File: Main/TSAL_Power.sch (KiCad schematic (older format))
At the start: 124 parts, among them Q10 NPN, Q11 MJD122, Q12 PNP, Q6 BSC0904NSI, Q7 BSC0902NSI, Q8 BSC0902NSI, Q9 MJD122, U10 TLV431, U11 TLV431, U4 TPS562200, U5 TPS63020, U6 MAX40200AUK, U7 INA180A3, U8 TLV9104, U9 LM25117

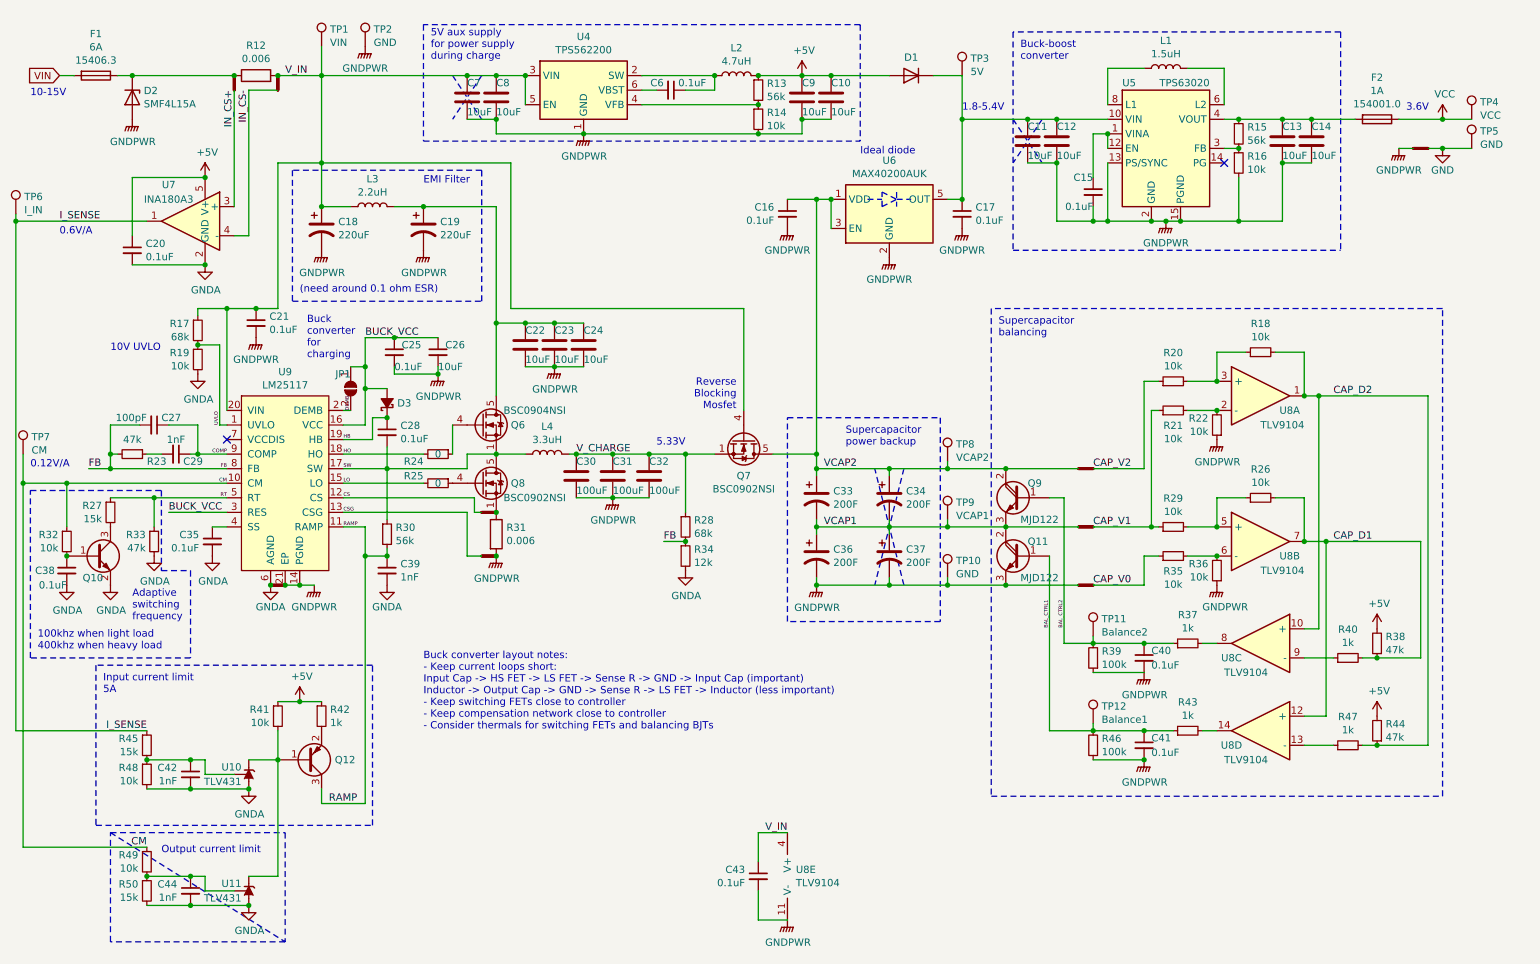
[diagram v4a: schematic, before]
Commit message: Main: optimized layout
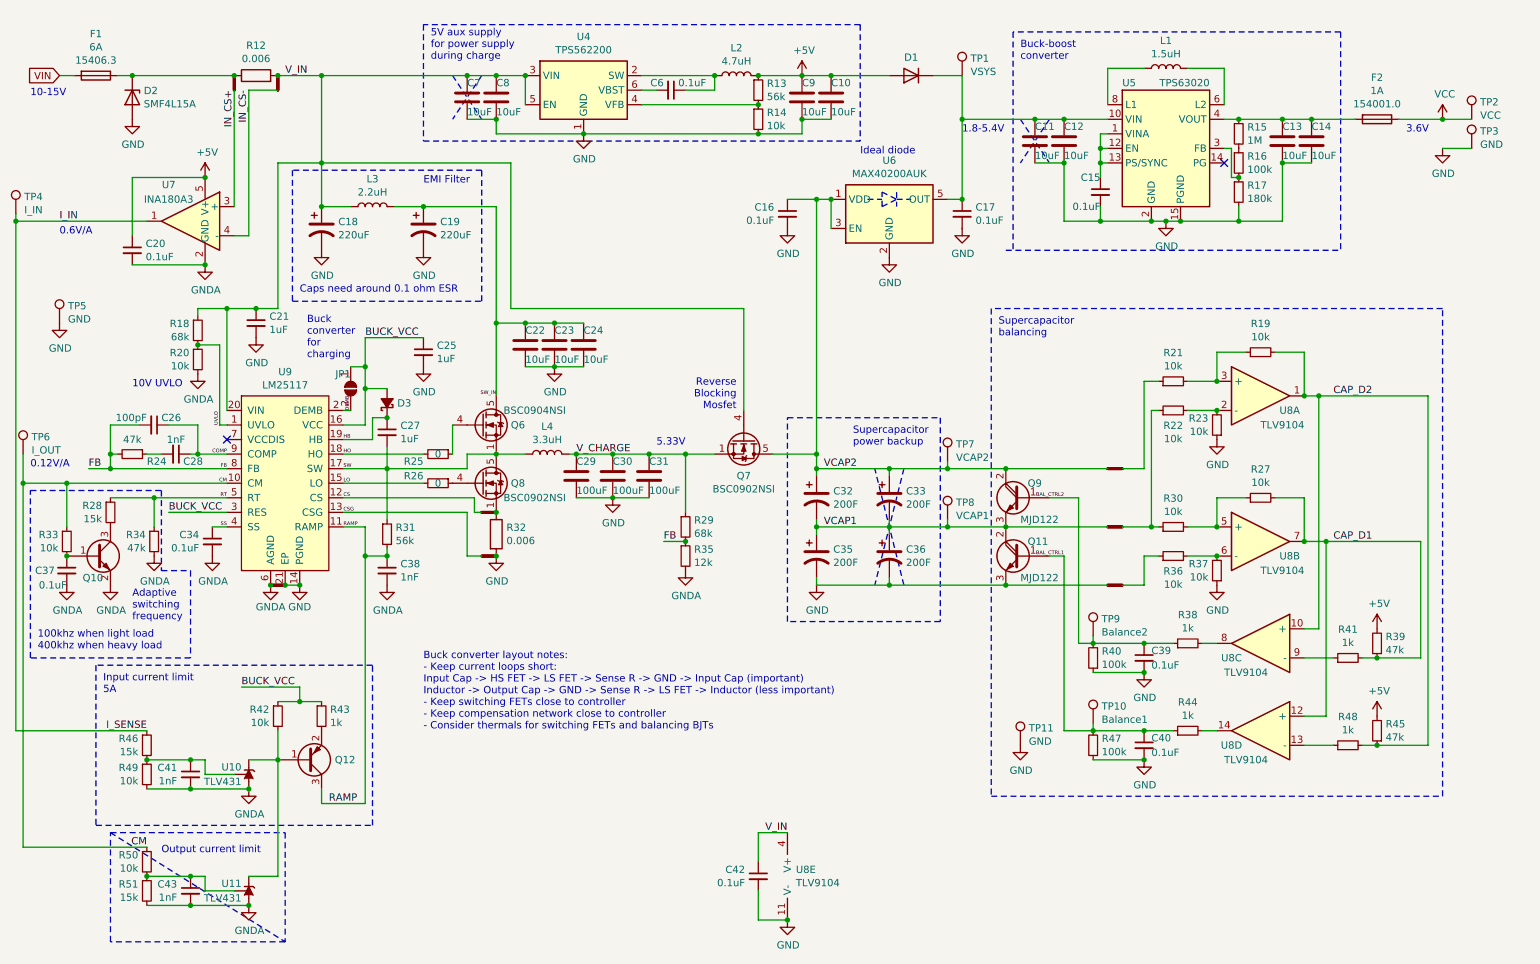
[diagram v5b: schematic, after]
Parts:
- removed C25, C28: 0.1uF, Capacitor_SMD:C_0402_1005Metric, symbol Device:C_Small
- removed TP1, TP10, TP2, TP9: ~, TestPoint:TestPoint_Loop_D2.50mm_Drill1.0mm, symbol Connector:TestPoint
- removed ZZ4, ZZ6, ZZ9: ~, project:Trace_0.2mmx0.6mm, symbol project:Wire
- added C27: 1uF, Capacitor_SMD:C_0402_1005Metric, symbol Device:C_Small
- added R16: 100k, Resistor_SMD:R_0805_2012Metric, symbol Device:R_Small
- added TP11, TP5, TP7: ~, TestPoint:TestPoint_Loop_D2.50mm_Drill1.0mm, symbol Connector:TestPoint
- added ZZ5, ZZ8: ~, project:Trace_0.2mmx0.6mm, symbol project:Wire
- C21: value 0.1uF -> 1uF; Comment (none) -> 25V
- C25: renamed from C26; value 10uF -> 1uF; footprint Capacitor_SMD:C_0805_2012Metric -> Capacitor_SMD:C_0402_1005Metric; Comment (none) -> 25V
- R13, R14: footprint Resistor_SMD:R_0805_2012Metric -> Resistor_SMD:R_0402_1005Metric
- R15: value 56k -> 1M
- R17: renamed from R16; value 10k -> 180k
- R20: renamed from R19; footprint Resistor_SMD:R_0805_2012Metric -> Resistor_SMD:R_0402_1005Metric
- R31: renamed from R30; footprint Resistor_SMD:R_0805_2012Metric -> Resistor_SMD:R_0402_1005Metric
- R49: renamed from R48; footprint Resistor_SMD:R_0805_2012Metric -> Resistor_SMD:R_0402_1005Metric
- R50: renamed from R49; footprint Resistor_SMD:R_0805_2012Metric -> Resistor_SMD:R_0402_1005Metric
- TP1: renamed from TP3; Comment 5V -> VSYS
- TP6: renamed from TP7; Comment CM -> I_OUT
- TP8: Comment VCAP2 -> VCAP1
- ZZ3: footprint project:Trace_1mmx2mm -> project:Trace_0.2mmx0.6mm
- ZZ7: renamed from ZZ8; footprint project:Trace_0.4mmx0.8mm -> project:Trace_0.2mmx0.6mm
- renumbered C27 to C26, C29 to C28, C30 to C29, C31 to C30, C32 to C31, C33 to C32, C34 to C33, C35 to C34, C36 to C35, C37 to C36, C38 to C37, C39 to C38, C40 to C39, C41 to C40, C42 to C41, C43 to C42, C44 to C43, R17 to R18, R18 to R19, R20 to R21, R21 to R22, R22 to R23, R23 to R24, R24 to R25, R25 to R26, R26 to R27, R27 to R28, R28 to R29, R29 to R30, R31 to R32, R32 to R33, R33 to R34, R34 to R35, R35 to R36, R36 to R37, R37 to R38, R38 to R39, R39 to R40, R40 to R41, R41 to R42, R42 to R43, R43 to R44, R44 to R45, R45 to R46, R46 to R47, R47 to R48, R50 to R51, TP12 to TP10, TP4 to TP2, TP5 to TP3, TP6 to TP4, TP11 to TP9, ZZ5 to ZZ4, ZZ7 to ZZ6
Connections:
- net +5V: no longer R42.1, R43.1
- net BUCK_VCC: now also R42.1, R43.1
- net GND: now also C10.2, C11.2, C12.2, C13.2, C14.2, C15.2, C16.2, C17.2, C18.2, C19.2, C21.2, C22.2, C23.2, C24.2, C25.2, C29.2, C30.2, C31.2, C35.2, C36.2, C39.2, C40.2, C42.2, C7.2, C8.2, C9.2, D2.2 (A), Q11.3 (E), R14.2, R17.2, R23.1, R32.2, R37.1, R40.1, R47.1, U4.1 (GND), U5.15 (PGND), U5.2 (GND), U6.2 (GND), U8.11 (V-), U9.14 (PGND), U9.21 (EP), ZZ6.2, ZZ7.2, TP11.1, TP5.1, ZZ8.1; no longer ZZ3.2
- net HB: now also C27.1
- net SW: now also C27.2
- net VCAP1: now also TP8.1, ZZ5.1
- net VCAP2: now also ZZ3.1, TP7.1; no longer TP8.1
- net SW_IN: now reaches C19.1, C22.1, C23.1, C24.1, L3.2, Q6.5 (D)
- net SS: now reaches C34.1, U9.4 (SS)
- net at C15.1, U5.1 (VINA), U5.12 (EN): now also U5.13 (PS/SYNC)
- net at R17.1, U5.3 (FB): now also R16.2; no longer R15.2
- net CAP_V0: no longer names the net of R36.1
- net CAP_V0: now also ZZ8.2
- net CAP_V1: no longer names the net of R22.1, R30.1
- net CAP_V1: now also ZZ5.2
- net CAP_V2: no longer names the net of R21.1
- net CAP_V2: now also ZZ3.2
- removed net GNDPWR: C10.2, C11.2, C12.2, C13.2, C14.2, C15.2, C16.2, C17.2, C18.2, C19.2, C21.2, C22.2, C23.2, C24.2, C25.2, C29.2, C30.2, C31.2, C35.2, C36.2, C39.2, C40.2, C42.2, C7.2, C8.2, C9.2, D2.2 (A), Q11.3 (E), R14.2, R17.2, R23.1, R32.2, R37.1, R40.1, R47.1, U4.1 (GND), U5.13 (PS/SYNC), U5.15 (PGND), U5.2 (GND), U6.2 (GND), U8.11 (V-), U9.14 (PGND), U9.21 (EP), ZZ3.1, ZZ6.2, ZZ7.2
- net I_SENSE renamed I_IN
- new net: R15.2, R16.1
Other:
- note added: "Caps need around 0.1 ohm ESR"
- note removed: "(need around 0.1 ohm ESR)"
- moved on the sheet: C11, C12, C15, C25, R17

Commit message: Main: fix rescue symbols
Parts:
- C18, C19, C32, C33, C35, C36: symbol TSAL-rescue:C_Polarized_US-Device -> Device:C_Polarized
- D3: symbol TSAL-rescue:D_Schottky_Small_Filled-Device -> Device:D_Schottky_Small_Filled
- U8: symbol TSAL-rescue:Opamp_Quad-Device -> Device:Opamp_Quad
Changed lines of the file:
@@
 $EndComp
 $Comp
-L TSAL-rescue:Opamp_Quad-Device U8
+L Device:Opamp_Quad U8
 U 3 1 616C69E2
 P 9250 5400
+AR Path="/616C69E2" Ref="U8"  Part="3"
+AR Path="/5DE07D62/616C69E2" Ref="U8"  Part="3"
 F 0 "U8" H 9450 5300 50  0000 C CNN
 F 1 "TLV9104" H 9350 5200 50  0000 C CNN
@@
 $EndComp
 $Comp
-L TSAL-rescue:Opamp_Quad-Device U8
+L Device:Opamp_Quad U8
 U 4 1 616C7F69
 P 9250 6000
+AR Path="/616C7F69" Ref="U8"  Part="4"
+AR Path="/5DE07D62/616C7F69" Ref="U8"  Part="4"
 F 0 "U8" H 9450 5900 50  0000 C CNN
 F 1 "TLV9104" H 9350 5800 50  0000 C CNN
@@
 $EndComp
 $Comp
-L TSAL-rescue:Opamp_Quad-Device U8
+L Device:Opamp_Quad U8
 U 2 1 616C4A34
 P 9250 4700
+AR Path="/616C4A34" Ref="U8"  Part="2"
+AR Path="/5DE07D62/616C4A34" Ref="U8"  Part="2"
 F 0 "U8" H 9450 4600 50  0000 C CNN
 F 1 "TLV9104" H 9400 4500 50  0000 C CNN
@@
 $EndComp
 $Comp
-L TSAL-rescue:Opamp_Quad-Device U8
+L Device:Opamp_Quad U8
 U 1 1 615ADA58
 P 9250 3700
+AR Path="/615ADA58" Ref="U8"  Part="1"
+AR Path="/5DE07D62/615ADA58" Ref="U8"  Part="1"
 F 0 "U8" H 9450 3600 50  0000 C CNN
 F 1 "TLV9104" H 9400 3500 50  0000 C CNN
@@
 $EndComp
 $Comp
-L TSAL-rescue:Opamp_Quad-Device U8
+L Device:Opamp_Quad U8
 U 5 1 616A1882
 P 6100 7000
+AR Path="/616A1882" Ref="U8"  Part="5"
+AR Path="/5DE07D62/616A1882" Ref="U8"  Part="5"
 F 0 "U8" H 6058 7046 50  0000 L CNN
 F 1 "TLV9104" H 6058 6955 50  0000 L CNN
@@
 $EndComp
 $Comp
-L TSAL-rescue:D_Schottky_Small_Filled-Device D3
+L Device:D_Schottky_Small_Filled D3
 U 1 1 602CFF2F
 P 3250 3750
+AR Path="/602CFF2F" Ref="D3"  Part="1"
+AR Path="/5DE07D62/602CFF2F" Ref="D3"  Part="1"
 F 0 "D3" V 3250 3680 50  0000 R CNN
 F 1 "~" V 3205 3680 50  0000 R CNN
@@
 $EndComp
 $Comp
-L TSAL-rescue:C_Polarized_US-Device C?
+L Device:C_Polarized C?
 U 1 1 60398AFC
 P 6200 4400
@@
 $EndComp
 $Comp
-L TSAL-rescue:C_Polarized_US-Device C?
+L Device:C_Polarized C?
 U 1 1 60399785
 P 6200 4800
@@
 $EndComp
 $Comp
-L TSAL-rescue:C_Polarized_US-Device C?
+L Device:C_Polarized C?
 U 1 1 6039DE0A
 P 6700 4400
@@
 $EndComp
 $Comp
-L TSAL-rescue:C_Polarized_US-Device C?
+L Device:C_Polarized C?
 U 1 1 6039DE10
 P 6700 4800
@@
 $EndComp
 $Comp
-L TSAL-rescue:C_Polarized_US-Device C?
+L Device:C_Polarized C?
 U 1 1 604522CD
 P 2800 2550
@@
 $EndComp
 $Comp
-L TSAL-rescue:C_Polarized_US-Device C?
+L Device:C_Polarized C?
 U 1 1 6136B917
 P 3500 2550

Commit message: Main: update sot23-5/6 footprints
Bloody kicad libaries
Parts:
- F1, F2: footprint footprints_archive_old_design:Fuseholder_Littelfuse_Nano2_154x -> Fuse:Fuseholder_Littelfuse_Nano2_154x
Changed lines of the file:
@@
 F 0 "F2" V 9763 1800 50  0000 C CNN
 F 1 "1A" V 9854 1800 50  0000 C CNN
-F 2 "footprints_archive_old_design:Fuseholder_Littelfuse_Nano2_154x" V 9980 1800 50  0001 C CNN
+F 2 "Fuse:Fuseholder_Littelfuse_Nano2_154x" V 9980 1800 50  0001 C CNN
 F 3 "~" H 10050 1800 50  0001 C CNN
 F 4 "154001.0" V 9945 1800 50  0000 C CNN "Part"
@@
 F 0 "F1" V 963 1500 50  0000 C CNN
 F 1 "6A" V 1054 1500 50  0000 C CNN
-F 2 "footprints_archive_old_design:Fuseholder_Littelfuse_Nano2_154x" V 1180 1500 50  0001 C CNN
+F 2 "Fuse:Fuseholder_Littelfuse_Nano2_154x" V 1180 1500 50  0001 C CNN
 F 3 "~" H 1250 1500 50  0001 C CNN
 F 4 "15406.3" V 1145 1500 50  0000 C CNN "Part"

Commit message: Main: archive symbols and footprints
Kicad library management is really terrible.
This is pulled together with janky scripts and sed.
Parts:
- C10, C11, C12, C13, C14, C9: footprint Capacitor_SMD:C_0805_2012Metric -> archive:C_0805_2012Metric; symbol Device:C -> archive:Device_C
- C15, C16, C17, C20, C21, C25, C26, C27, C28, C34, C37, C38, C39, C40, C41, C42, C43, C6: footprint Capacitor_SMD:C_0402_1005Metric -> archive:C_0402_1005Metric; symbol Device:C_Small -> archive:Device_C_Small
- C18, C19: footprint Capacitor_SMD:CP_Elec_8x10.5 -> archive:CP_Elec_8x10.5; symbol Device:C_Polarized -> archive:Device_C_Polarized
- C22, C23, C24, C29, C30, C31, C7, C8: footprint Capacitor_SMD:C_1210_3225Metric -> archive:C_1210_3225Metric; symbol Device:C -> archive:Device_C
- C32, C33, C35, C36: footprint Capacitor_THT:CP_Radial_D30.0mm_P10.00mm_SnapIn -> archive:CP_Radial_D30.0mm_P10.00mm_SnapIn; symbol Device:C_Polarized -> archive:Device_C_Polarized
- D1: footprint Diode_SMD:D_SOD-123 -> archive:D_SOD-123; symbol Device:D -> archive:Device_D
- D2: footprint Diode_SMD:D_SOD-123 -> archive:D_SOD-123; symbol Device:D_Zener -> archive:Device_D_Zener
- D3: footprint Diode_SMD:D_SOD-323 -> archive:D_SOD-323; symbol Device:D_Schottky_Small_Filled -> archive:Device_D_Schottky_Small_Filled
- F1, F2: footprint Fuse:Fuseholder_Littelfuse_Nano2_154x -> archive:Fuseholder_Littelfuse_Nano2_154x; symbol Device:Fuse -> archive:Device_Fuse
- JP1: footprint Resistor_SMD:R_0402_1005Metric -> archive:R_0402_1005Metric; symbol Jumper:SolderJumper_2_Open -> archive:Jumper_SolderJumper_2_Open
- L1, L2: footprint Inductor_SMD:L_Bourns-SRN4018 -> archive:L_Bourns-SRN4018; symbol Device:L -> archive:Device_L
- L3: footprint Inductor_SMD:L_Bourns-SRN8040_8x8.15mm -> archive:L_Bourns-SRN8040_8x8.15mm; symbol Device:L -> archive:Device_L
- L4: footprint Inductor_SMD:L_Bourns_SRP1245A -> archive:L_Bourns_SRP1245A; symbol Device:L -> archive:Device_L
- Q10: footprint Package_TO_SOT_SMD:SOT-23 -> archive:SOT-23; symbol Device:Q_NPN_BEC -> archive:Device_Q_NPN_BEC
- Q11, Q9: footprint Package_TO_SOT_SMD:TO-252-2 -> archive:TO-252-2; symbol Device:Q_NPN_Darlington_BCE -> archive:Device_Q_NPN_Darlington_BCE
- Q12: footprint Package_TO_SOT_SMD:SOT-23 -> archive:SOT-23; symbol Device:Q_PNP_BEC -> archive:Device_Q_PNP_BEC
- Q6, Q7, Q8: footprint Package_TO_SOT_SMD:TDSON-8-1 -> archive:TDSON-8-1; symbol project:NMOS_SuperSO8 -> archive:project_NMOS_SuperSO8
- R12, R32: footprint Resistor_SMD:R_2512_6332Metric -> archive:R_2512_6332Metric; symbol Device:R -> archive:Device_R
- R13, R14, R19, R20, R21, R22, R23, R24, R25, R26, R27, R30, R31, R33, R34, R36, R37, R38, R39, R40, R41, R42, R43, R44, R45, R47, R48, R49, R50: footprint Resistor_SMD:R_0402_1005Metric -> archive:R_0402_1005Metric; symbol Device:R_Small -> archive:Device_R_Small
- R15, R16, R17, R18, R28, R29, R35, R46, R51: footprint Resistor_SMD:R_0805_2012Metric -> archive:R_0805_2012Metric; symbol Device:R_Small -> archive:Device_R_Small
- TP1, TP10, TP11, TP2, TP3, TP4, TP5, TP6, TP7, TP8, TP9: footprint TestPoint:TestPoint_Loop_D2.50mm_Drill1.0mm -> archive:TestPoint_Loop_D2.50mm_Drill1.0mm; symbol Connector:TestPoint -> archive:Connector_TestPoint
- U10, U11: footprint Package_TO_SOT_SMD:SOT-23 -> archive:SOT-23; symbol Reference_Voltage:TL432DBZ -> archive:Reference_Voltage_TL432DBZ
- U4: footprint Package_TO_SOT_SMD:SOT-23-6 -> archive:SOT-23-6; symbol Regulator_Switching:TPS562200 -> archive:Regulator_Switching_TPS562200
- U5: footprint project:TPS63020 -> archive:TPS63020; symbol project:TPS63020 -> archive:project_TPS63020
- U6: footprint Package_TO_SOT_SMD:SOT-23-5 -> archive:SOT-23-5; symbol Analog_Switch:MAX40200AUK -> archive:Analog_Switch_MAX40200AUK
- U7: footprint Package_TO_SOT_SMD:SOT-23-5 -> archive:SOT-23-5; symbol project:INA180A -> archive:project_INA180A
- U8: footprint Package_SO:TSSOP-14_4.4x5mm_P0.65mm -> archive:TSSOP-14_4.4x5mm_P0.65mm; symbol Device:Opamp_Quad -> archive:Device_Opamp_Quad
- U9: footprint Package_SO:ETSSOP-20-1EP_4.4x6.5mm_P0.65mm_EP3x4.2mm -> archive:ETSSOP-20-1EP_4.4x6.5mm_P0.65mm_EP3x4.2mm; symbol project:LM5117PMH -> archive:project_LM5117PMH
- ZZ1, ZZ2, ZZ3, ZZ4, ZZ5, ZZ6, ZZ7, ZZ8: footprint project:Trace_0.2mmx0.6mm -> archive:Trace_0.2mmx0.6mm; symbol project:Wire -> archive:project_Wire
